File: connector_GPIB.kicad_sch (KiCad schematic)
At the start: 1 part, among them J1201 NorComp - 112-024-113RYY1

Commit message: More wiring - Ethernet, SPI flash
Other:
- note added: "LOGIC_GND"
- note added: "Shield"
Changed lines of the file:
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@@
+		)
+	)
+	(text "Shield"
+		(exclude_from_sim no)
+		(at 132.08 96.52 0)
+		(effects
+			(font
+				(size 1.27 1.27)
+			)
+			(justify right bottom)
+		)
+	)
+	(text "LOGIC_GND"
+		(exclude_from_sim no)
+		(at 144.78 96.52 0)
+		(effects
+			(font
+				(size 1.27 1.27)
+			)
+			(justify left bottom)
 		)
 	)

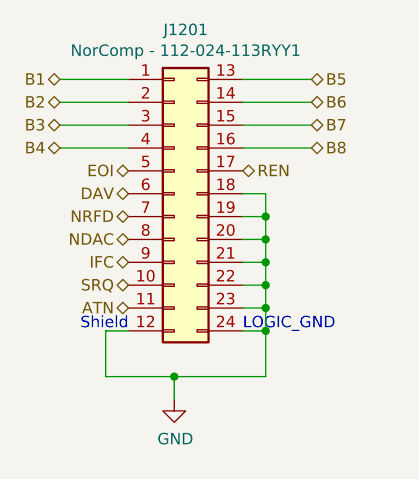
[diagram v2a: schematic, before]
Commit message: partial! Ran wires for GPIB connector
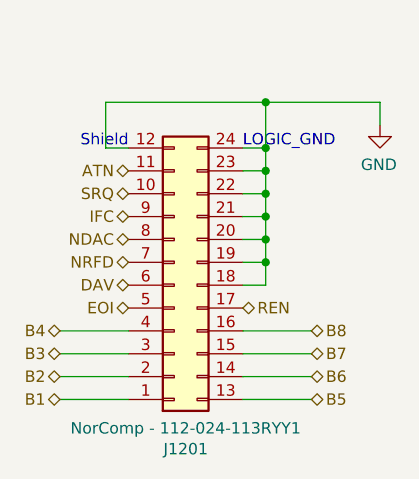
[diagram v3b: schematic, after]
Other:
- moved on the sheet: J1201

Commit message: Add order codes for all components
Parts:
- J1201: JLCPCB_IGNORE (none) -> 1
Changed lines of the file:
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@@
+			)
+		)
+		(property "I2C address" ""
+			(at 137.16 91.44 0)
+			(effects
+				(font
+					(size 1.27 1.27)
+				)
+				(hide yes)
+			)
+		)
+		(property "JLCPCB_IGNORE" "1"
+			(at 137.16 91.44 0)
+			(effects
+				(font
+					(size 1.27 1.27)
+				)
+				(hide yes)
 			)
 		)

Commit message: Silkscreen work. Edit tittle block/version number
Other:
- company: (c) -> (c) Vincent Dalstra
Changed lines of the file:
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@@
 	(title_block
 		(title "Untitled 4-layer JLCPCB")
-		(date "1984/04/01")
-		(rev "v1.0.0")
-		(company "(c)")
+		(date "2024-06-14")
+		(rev "1.0.0")
+		(company "(c) Vincent Dalstra")
 	)
 	(junction
